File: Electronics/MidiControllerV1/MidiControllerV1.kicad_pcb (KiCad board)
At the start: 2 copper layers, 134 x 28 mm, 14 parts, among them J2 KeypadConnector, J3 OledConnector, J4 BluePillHeaderA, J5 BluepillHeaderB, SW1 Rotary_Encoder_Switch, SW2 Rotary_Encoder_Switch

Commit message: #24 Laid out pcb
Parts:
- moved J2 23.0 mm to (88.5, 42.0), turned to 270 degrees
- moved R1 0.12 mm to (25.5, 43.5)
- moved R3 0.10 mm to (30.5, 43.5)
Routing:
- net ENC2_SW: track 0.00 -> 101.7 mm
- net ENC1A: track 0.00 -> 96.3 mm
- net ENC2A: track 0.00 -> 94.9 mm
- net ENC1_SW: track 0.00 -> 90.7 mm, vias 0 -> 1
- net ENC1B: track 0.00 -> 87.7 mm
- net ENC2B: track 0.00 -> 84.6 mm
- net KP_C1: track 0.00 -> 80.7 mm
- net KP_C4: track 0.00 -> 80.0 mm
- net KP_C3: track 0.00 -> 80.0 mm
- net KP_C2: track 0.00 -> 80.0 mm
- net +3V3: track 0.00 -> 65.4 mm
- net LCD_SCL: track 0.00 -> 65.3 mm
- net LCD_SDA: track 0.00 -> 62.5 mm
- net KP_R4: track 0.00 -> 48.0 mm
- net KP_R3: track 0.00 -> 42.5 mm
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
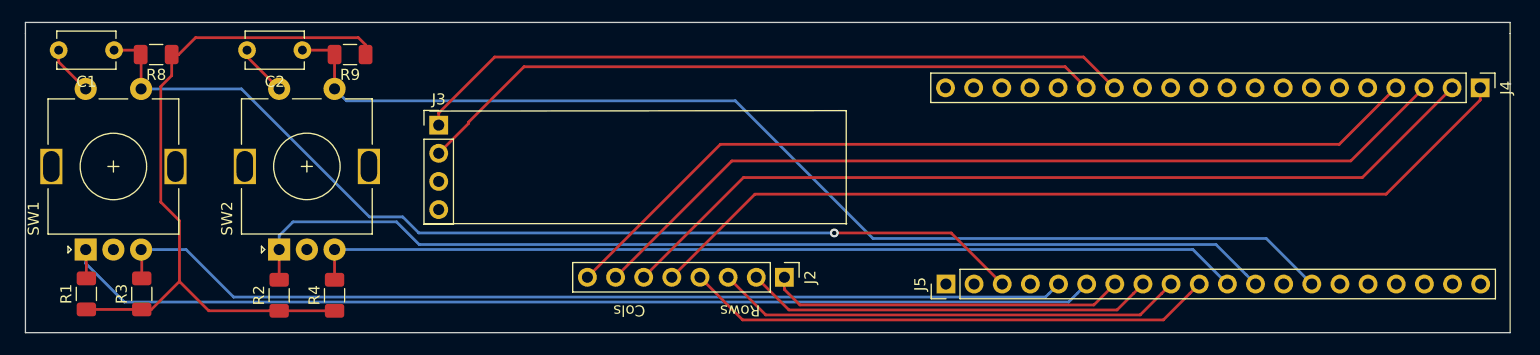
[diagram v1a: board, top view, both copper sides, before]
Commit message: Finished PCB layout
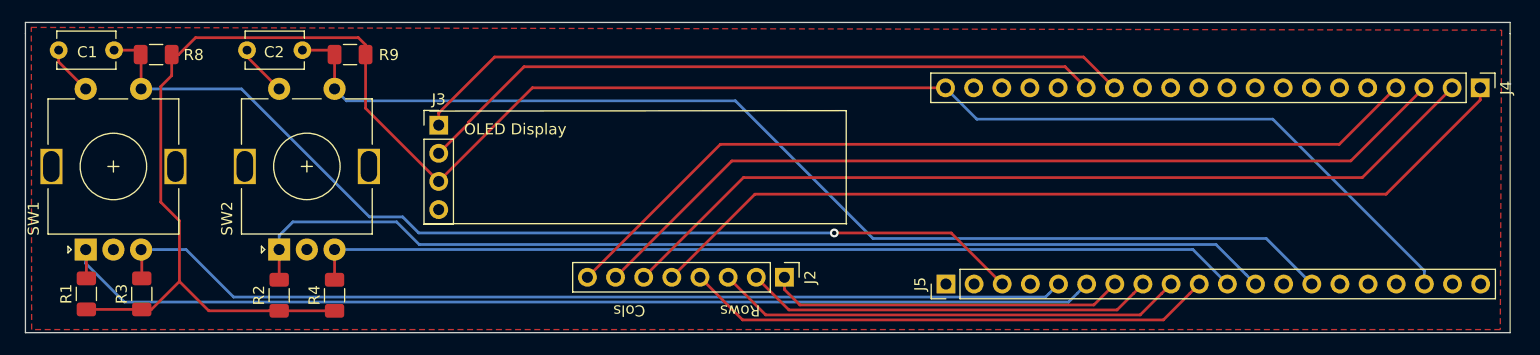
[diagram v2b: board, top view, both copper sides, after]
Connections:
- J3 pad 3: +5V -> +3V3
- J4 pad 19: GNDREF -> GND
- J5 pad 19: GNDREF -> GND
- J5 pad 20: GNDREF -> GND
- SW1 pad MP: (no net) -> GND
- SW2 pad MP: (no net) -> GND
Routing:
- net +3V3: track 65.4 -> 180.1 mm
- added copper zone on F.Cu, net GND
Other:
- board text added: "OLED Display"
